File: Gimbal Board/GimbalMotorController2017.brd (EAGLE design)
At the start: 83.4 x 72.1 mm, 123 parts, among them J1 SL03THROUGH_HOLE, J3 APP_2POS_CONFIG5V_HORIZ, Q1 Q_IRF7437SMD, Q2 Q_IRF7437SMD, Q3 Q_IRF7437SMD, Q4 Q_IRF7437SMD, Q5 Q_IRF7437SMD, Q6 Q_IRF7437SMD, Q7 MOSFET-PCHANNEL, Q8 MOSFET-PCHANNEL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

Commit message: Added Vertical Mounting Wing. Integrated New Fets adjusted andersons for Control Card
0.5 Inches of the Board has been added for a vertical mounting wing. Routing for new fets has been made. Board has been increased in size significantly. Basic Silkscreen adjustments have been made. Board should be ready for Rev 1.
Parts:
- moved Q6 226.1 mm to (83.8, 28.4), turned to 270 degrees
- moved Q5 212.4 mm to (83.8, 38.9), turned to 270 degrees
- moved Q4 206.5 mm to (83.8, 57.9), turned to 270 degrees
- moved Q3 193.5 mm to (83.8, 68.6), turned to 270 degrees
- moved Q2 165.9 mm to (61.2, 75.9)
- moved Q1 163.3 mm to (78.5, 87.4), turned to 270 degrees
- moved U$9 102.4 mm to (13.3, -11.5)
- moved C37 80.6 mm to (22.9, 73.9), turned to 270 degrees
- moved C15 49.6 mm to (46.5, 74.2)
- moved U$28 30.6 mm to (52.6, 83.6)
- moved U$29 20.9 mm to (20.3, 83.6)
- moved U$5 14.2 mm to (105.7, 77.0)
- moved J3 7.62 mm to (113.3, 9.75)
- moved U$6 5.85 mm to (105.7, 47.2)
- moved U$7 3.59 mm to (105.7, 18.0)
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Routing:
- net N$14: track 6.25 -> 80.6 mm
- net N$16: track 4.14 -> 35.6 mm
- net N$13: track 7.51 -> 32.2 mm
- net N$15: track 4.92 -> 28.0 mm
- net N$18: track 4.62 -> 24.1 mm
- net N$17: track 5.47 -> 24.6 mm
- net SH_A: track 82.3 -> 101.1 mm, vias 4 -> 5
- net PVDD: track 60.8 -> 79.1 mm, vias 5 -> 8
- net SL_A: track 69.8 -> 83.7 mm
- net SL_B: track 53.1 -> 63.2 mm
- net SH_B: track 71.4 -> 79.1 mm, vias 2 -> 4
- net N$31: track 45.3 -> 47.7 mm
- net SH_C: track 87.3 -> 85.2 mm, vias 2 -> 3
- net VCC: track 214.7 -> 212.8 mm
- net N$29: track 37.9 -> 39.2 mm
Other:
- board size 83.4 x 72.1 mm -> 86.5 x 99.8 mm
- board text added: "Gimball Powerboard Mars Rover Design Team 2018 Rev 1 University of Missouri Science and Technology Evan Hite Shaun McManus"

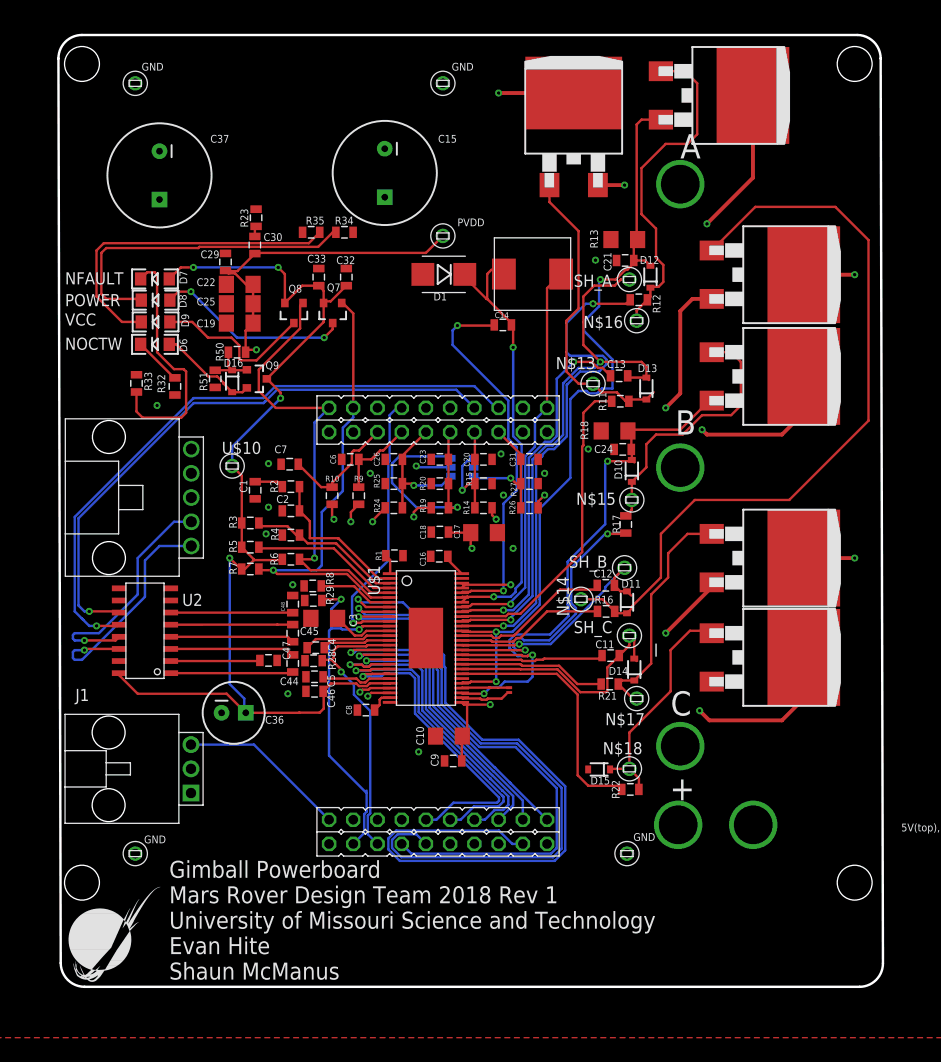
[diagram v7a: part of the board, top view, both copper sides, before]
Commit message: Added Vertical mounting wing
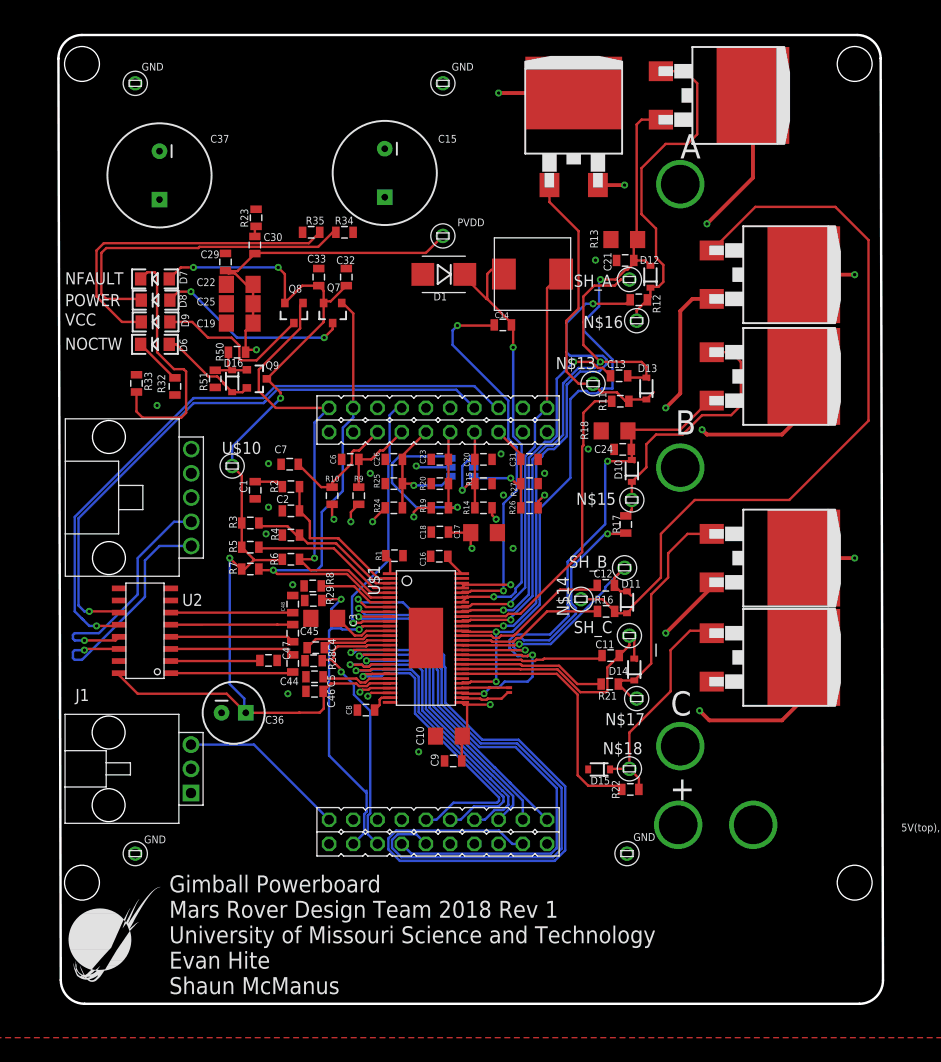
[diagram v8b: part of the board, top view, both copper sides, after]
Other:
- board size 86.5 x 99.8 mm -> 86.5 x 101.6 mm
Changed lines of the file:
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@@
 <board>
 <plain>
-<wire x1="12.2617875" y1="86.165259375" x2="12.503146875" y2="-8.679471875" width="0.254" layer="20"/>
-<wire x1="12.503146875" y1="-8.679471875" x2="15.00641875" y2="-11.176" width="0.254" layer="20" curve="89.85423"/>
-<wire x1="15.00641875" y1="-11.176" x2="96.264196875" y2="-11.176" width="0.254" layer="20"/>
-<wire x1="96.264196875" y1="-11.176" x2="98.723725" y2="-8.710171875" width="0.254" layer="20" curve="90.146543"/>
-<wire x1="98.723725" y1="-8.710171875" x2="98.48225625" y2="86.177540625" width="0.254" layer="20"/>
+<wire x1="12.2617875" y1="86.165259375" x2="12.507690625" y2="-10.46484375" width="0.254" layer="20"/>
+<wire x1="12.507690625" y1="-10.46484375" x2="15.0031125" y2="-12.954" width="0.254" layer="20" curve="89.854202"/>
+<wire x1="15.0031125" y1="-12.954" x2="96.26085625" y2="-12.954" width="0.254" layer="20"/>
+<wire x1="96.26085625" y1="-12.954" x2="98.72823125" y2="-10.48080625" width="0.254" layer="20" curve="90.134974"/>
+<wire x1="98.72823125" y1="-10.48080625" x2="98.48225625" y2="86.177540625" width="0.254" layer="20"/>
 <wire x1="98.48225625" y1="86.177540625" x2="96.017625" y2="88.636" width="0.254" layer="20" curve="89.854269"/>
 <wire x1="96.017625" y1="88.636" x2="14.72633125" y2="88.636" width="0.254" layer="20"/>
@@
 <text x="69.596" y="16.256" size="1.27" layer="21">N$17</text>
 <text x="66.294" y="25.908" size="1.27" layer="21">SH_C</text>
-<dimension x1="98.806" y1="1.524" x2="20.32" y2="-11.176" x3="98.552" y3="-4.826" textsize="1.778" layer="21" dtype="vertical" unit="inch"/>
-<text x="23.876" y="-10.414" size="1.778" layer="21" font="vector">Gimball Powerboard
+<text x="23.876" y="-11.938" size="1.778" layer="21" font="vector">Gimball Powerboard
 Mars Rover Design Team 2018 Rev 1
 University of Missouri Science and Technology
